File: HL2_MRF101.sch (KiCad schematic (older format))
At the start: 214 parts, among them J1 Antenna, J10 DB1, J2 HL2, J3 RF3, J4 RF1, J5 RCJ-041, J6 50VDC, J7 12V, J8 Fan, J9 HL2_12V, K1 EC2-3NU, K10 EC2-3NU, K11 EC2-3NU, K12 EC2-3NU, K13 EC2-3NU, K2 EC2-3NU, K3 EC2-3NU, K4 EC2-3NU, K5 EC2-3NU, K6 EC2-3NU, K7 EC2-3NU, K8 EC2-3NU, K9 EC2-3NU, Q1 MRF101AN, Q2 2N7002, Q3 IRLML6402, Q4 DTC144E, T1 Coupler, T2 Coupler, T3 744851330, U1 MCP6282E/MS, U2 MAX11645, U3 MCP23008, U4 ULN2003, U5 LM35-NEB, U6 MCP4561, U7 INA193

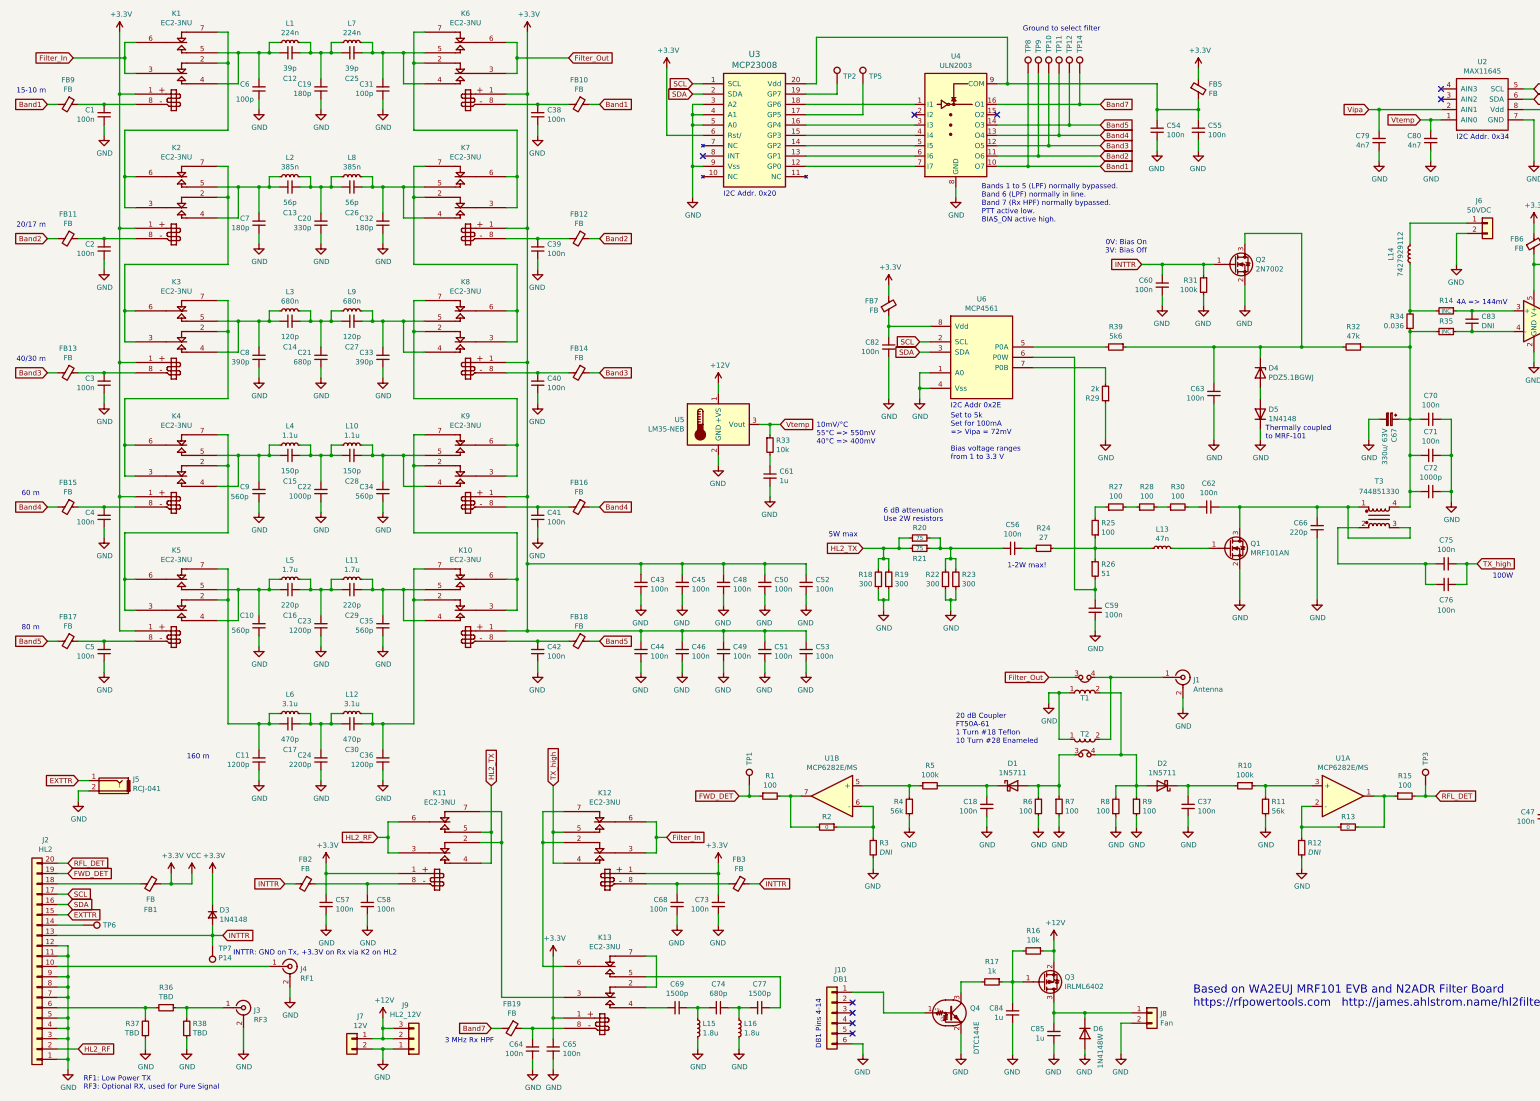
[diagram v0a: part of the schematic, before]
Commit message: Rx antenna change
RX antenna routed through HL2 rx antenna connection. High power tx tracks thickened to 2 mm and net list added for 50 ohm impedance top and bottom tracks for clearance.
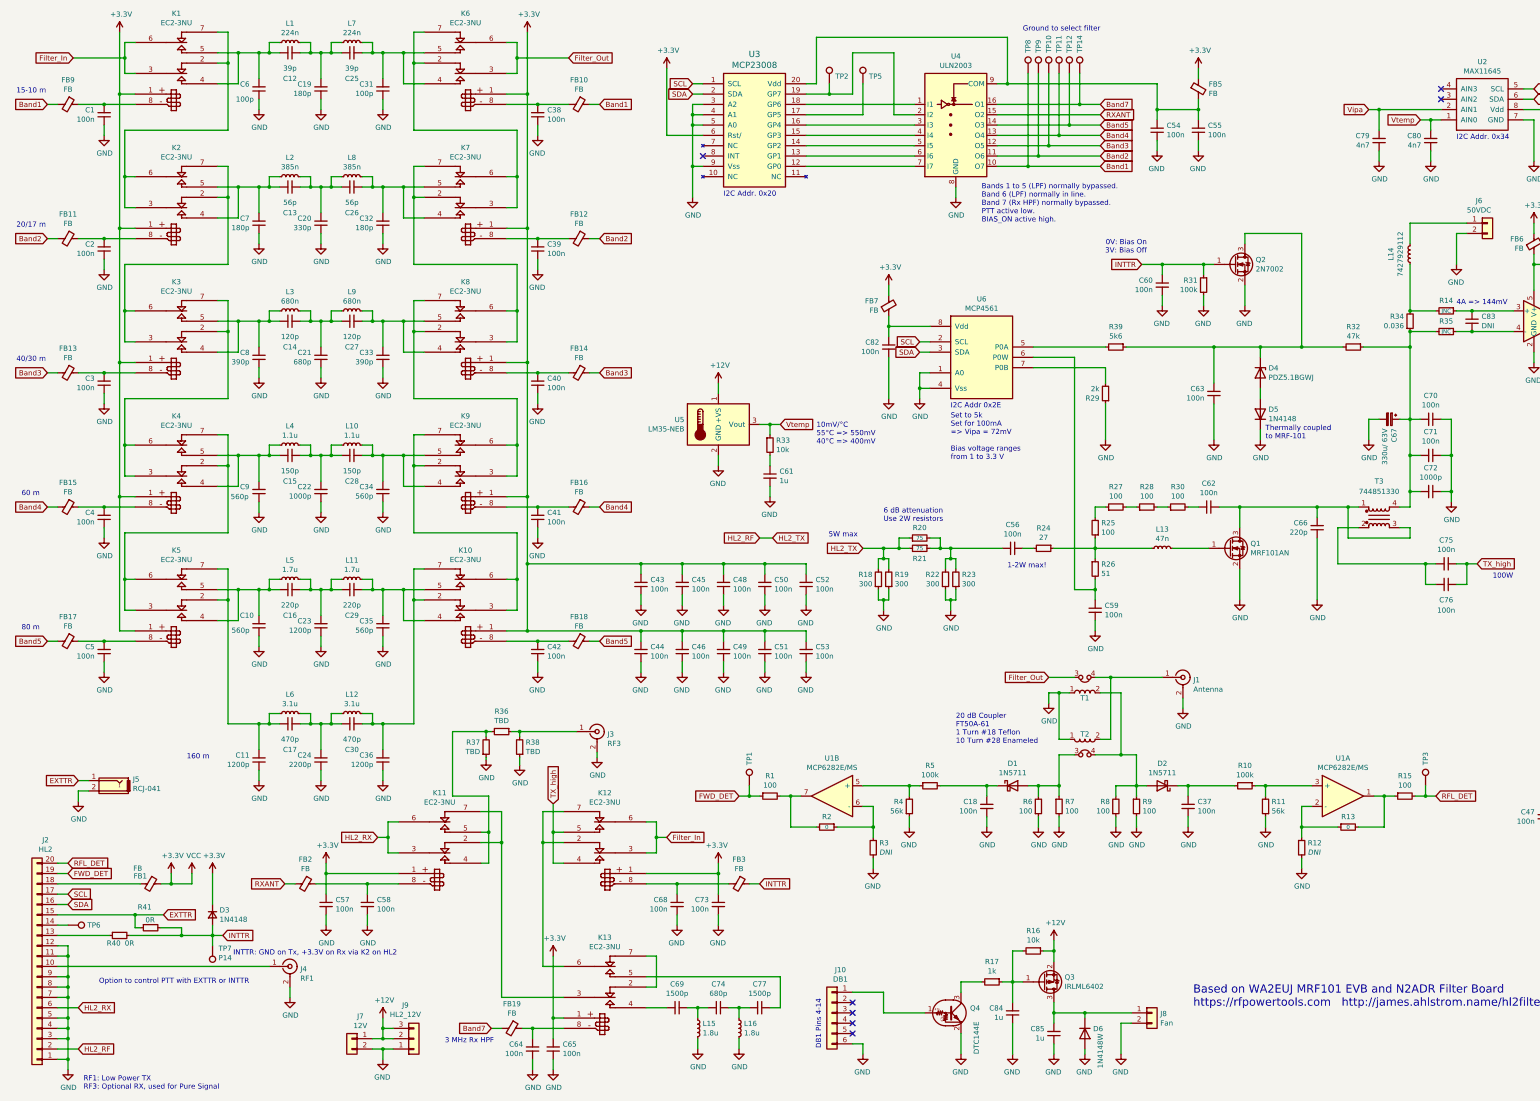
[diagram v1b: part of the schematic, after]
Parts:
- added R40, R41: 0R, Resistor_SMD:R_0603_1608Metric, symbol HL2_MRF101-rescue:R_Small-Device
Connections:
- net EXTTR: now also R41.1
- net HL2_RF: now also R18.2, R19.2, R20.1, R21.2; no longer K11.3, K11.6
- net INTTR: now also R40.2, R41.2; no longer FB2.2, J2.13 (Pin_13)
- net at R36.2, R37.2: now also K11.4, K11.5; no longer J2.6 (Pin_6)
- net at TP2.1, U3.19 (GP7): now also U4.2 (I2)
- net RXANT: now reaches U4.15 (O2)
- net RXANT: now also FB2.2
- removed net HL2_TX: K11.4, K11.5, R18.2, R19.2, R20.1, R21.2
- new net: J2.13 (Pin_13), R40.1
- new net HL2_RX: J2.6 (Pin_6), K11.3, K11.6
- no-connect marks 9 -> 7
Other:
- note added: "Option to control PTT with EXTTR or INTTR"
- moved on the sheet: J3, R36, R37, R38, TP2, TP6
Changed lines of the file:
@@
 Wire Wire Line
 	4100 8700 4100 8850
-Text GLabel 4000 8700 0    50   Input ~ 0
+Text GLabel 7700 5800 0    50   Input ~ 0
 HL2_RF
 Wire Wire Line
-	5000 8950 5100 8950
-Wire Wire Line
-	5100 8950 5100 8650
-Wire Wire Line
-	5100 8650 5000 8650
-Wire Wire Line
-	5100 8650 5100 8200
-Connection ~ 5100 8650
-Wire Wire Line
 	5800 8950 5700 8950
 Wire Wire Line
@@
 	5700 8650 5800 8650
 Wire Wire Line
-	5700 8650 5700 8200
+	5700 8650 5700 8375
 Connection ~ 5700 8650
 Wire Wire Line
@@
 Text GLabel 6800 8700 2    50   Input ~ 0
 Filter_In
-Text GLabel 5700 8200 1    50   Input ~ 0
+Text GLabel 5700 8375 1    50   Input ~ 0
 TX_high
-Text GLabel 5100 8200 1    50   Input ~ 0
+Text GLabel 7825 5800 2    50   Input ~ 0
 HL2_TX
 $Comp
@@
 $EndComp
 Text GLabel 3100 9150 0    50   Input ~ 0
-INTTR
+RXANT
 Wire Wire Line
 	3100 9150 3200 9150
@@
 SCL
 Wire Wire Line
-	900  9450 1000 9450
-Text GLabel 1000 9450 2    50   Input ~ 0
+	900  9450 1650 9450
+Text GLabel 1925 9450 2    50   Input ~ 0
 EXTTR
 $Comp
 L HL2_MRF101-rescue:TestPoint-Connector TP6
 U 1 1 60ED725B
-P 1150 9550
-F 0 "TP6" V 1150 9738 50  0000 L CNN
-F 1 "P8" V 1195 9738 50  0001 L CNN
-F 2 "TestPoint:TestPoint_Pad_D1.5mm" H 1350 9550 50  0001 C CNN
-F 3 "~" H 1350 9550 50  0001 C CNN
-	1    1150 9550
+P 1000 9550
+F 0 "TP6" V 1000 9738 50  0000 L CNN
+F 1 "P8" V 1045 9738 50  0001 L CNN
+F 2 "TestPoint:TestPoint_Pad_D1.5mm" H 1200 9550 50  0001 C CNN
+F 3 "~" H 1200 9550 50  0001 C CNN
+	1    1000 9550
 	0    1    1    0
 $EndComp
 Wire Wire Line
-	900  9550 1150 9550
+	900  9550 1000 9550
 $Comp
 L HL2_MRF101-rescue:TestPoint-Connector TP7
@@
 U 1 1 6126D5A4
 P 1800 9150
-F 0 "FB1" V 2050 9150 50  0000 C CNN
-F 1 "FB" V 1950 9150 50  0000 C CNN
+F 0 "FB1" V 1725 9050 50  0000 C CNN
+F 1 "FB" V 1650 9025 50  0000 C CNN
 F 2 "Inductor_SMD:L_0805_2012Metric" V 1730 9150 50  0001 C CNN
 F 3 "~" H 1800 9150 50  0001 C CNN
@@
 Wire Wire Line
 	900  9150 1700 9150
-Wire Wire Line
-	900  9650 2400 9650
 $Comp
 L HL2_MRF101-rescue:Conn_Coaxial-Connector J3
 U 1 1 5ECA38D8
-P 2700 10350
-F 0 "J3" H 2800 10325 50  0000 L CNN
-F 1 "RF3" H 2800 10234 50  0000 L CNN
-F 2 "n2adr:U.FL_Hirose_U.FL-R-SMT-1_Vertical" H 2700 10350 50  0001 C CNN
-F 3 " ~" H 2700 10350 50  0001 C CNN
-	1    2700 10350
+P 6125 7675
+F 0 "J3" H 6225 7650 50  0000 L CNN
+F 1 "RF3" H 6225 7559 50  0000 L CNN
+F 2 "n2adr:U.FL_Hirose_U.FL-R-SMT-1_Vertical" H 6125 7675 50  0001 C CNN
+F 3 " ~" H 6125 7675 50  0001 C CNN
+	1    6125 7675
 	1    0    0    -1
 $EndComp
@@
 Wire Wire Line
 	10800 1600 11000 1600
-NoConn ~ 10000 1700
-NoConn ~ 9200 1700
 Text Notes 8250 4900 0    50   ~ 0
 10mV/°C\n55°C => 550mV\n40°C => 400mV
@@
 L HL2_MRF101-rescue:R_Small-device R36
 U 1 1 5F471469
-P 1950 10350
-F 0 "R36" V 1754 10350 50  0000 C CNN
-F 1 "TBD" V 1845 10350 50  0000 C CNN
-F 2 "Resistor_SMD:R_0805_2012Metric" H 1950 10350 50  0001 C CNN
-F 3 "~" H 1950 10350 50  0001 C CNN
-	1    1950 10350
+P 5200 7675
+F 0 "R36" V 5004 7675 50  0000 C CNN
+F 1 "TBD" V 5095 7675 50  0000 C CNN
+F 2 "Resistor_SMD:R_0805_2012Metric" H 5200 7675 50  0001 C CNN
+F 3 "~" H 5200 7675 50  0001 C CNN
+	1    5200 7675
 	0    1    1    0
 $EndComp
@@
 L HL2_MRF101-rescue:R_Small-device R38
 U 1 1 5F4733D9
-P 2150 10550
-F 0 "R38" H 2091 10504 50  0000 R CNN
-F 1 "TBD" H 2091 10595 50  0000 R CNN
-F 2 "Resistor_SMD:R_0805_2012Metric" H 2150 10550 50  0001 C CNN
-F 3 "~" H 2150 10550 50  0001 C CNN
-	1    2150 10550
+P 5375 7825
+F 0 "R38" H 5316 7779 50  0000 R CNN
+F 1 "TBD" H 5316 7870 50  0000 R CNN
+F 2 "Resistor_SMD:R_0805_2012Metric" H 5375 7825 50  0001 C CNN
+F 3 "~" H 5375 7825 50  0001 C CNN
+	1    5375 7825
 	-1   0    0    1
 $EndComp
@@
 L HL2_MRF101-rescue:R_Small-device R37
 U 1 1 5F47390A
-P 1750 10550
-F 0 "R37" H 1692 10504 50  0000 R CNN
-F 1 "TBD" H 1692 10595 50  0000 R CNN
-F 2 "Resistor_SMD:R_0805_2012Metric" H 1750 10550 50  0001 C CNN
-F 3 "~" H 1750 10550 50  0001 C CNN
-	1    1750 10550
+P 5050 7825
+F 0 "R37" H 4992 7779 50  0000 R CNN
+F 1 "TBD" H 4992 7870 50  0000 R CNN
+F 2 "Resistor_SMD:R_0805_2012Metric" H 5050 7825 50  0001 C CNN
+F 3 "~" H 5050 7825 50  0001 C CNN
+	1    5050 7825
 	1    0    0    1
 $EndComp
@@
 L power:GND #PWR066
 U 1 1 5ECA38E2
-P 2700 10750
-F 0 "#PWR066" H 2700 10500 50  0001 C CNN
-F 1 "GND" H 2705 10577 50  0000 C CNN
-F 2 "" H 2700 10750 50  0001 C CNN
-F 3 "" H 2700 10750 50  0001 C CNN
-	1    2700 10750
+P 6125 7925
+F 0 "#PWR066" H 6125 7675 50  0001 C CNN
+F 1 "GND" H 6130 7752 50  0000 C CNN
+F 2 "" H 6125 7925 50  0001 C CNN
+F 3 "" H 6125 7925 50  0001 C CNN
+	1    6125 7925
 	1    0    0    -1
 $EndComp
@@
 L power:GND #PWR0107
 U 1 1 5F52250E
-P 2150 10750
-F 0 "#PWR0107" H 2150 10500 50  0001 C CNN
-F 1 "GND" H 2155 10577 50  0000 C CNN
-F 2 "" H 2150 10750 50  0001 C CNN
-F 3 "" H 2150 10750 50  0001 C CNN
-	1    2150 10750
+P 5375 8000
+F 0 "#PWR0107" H 5375 7750 50  0001 C CNN
+F 1 "GND" H 5380 7827 50  0000 C CNN
+F 2 "" H 5375 8000 50  0001 C CNN
+F 3 "" H 5375 8000 50  0001 C CNN
+	1    5375 8000
 	1    0    0    -1
 $EndComp
 Wire Wire Line
-	2150 10650 2150 10750
+	5375 7925 5375 8000
 $Comp
 L power:GND #PWR0109
 U 1 1 5F5D17C4
-P 1750 10750
-F 0 "#PWR0109" H 1750 10500 50  0001 C CNN
-F 1 "GND" H 1755 10577 50  0000 C CNN
-F 2 "" H 1750 10750 50  0001 C CNN
-F 3 "" H 1750 10750 50  0001 C CNN
-	1    1750 10750
+P 5050 7950
+F 0 "#PWR0109" H 5050 7700 50  0001 C CNN
+F 1 "GND" H 5055 7777 50  0000 C CNN
+F 2 "" H 5050 7950 50  0001 C CNN
+F 3 "" H 5050 7950 50  0001 C CNN
+	1    5050 7950
 	1    0    0    -1
 $EndComp
 Wire Wire Line
-	1750 10650 1750 10750
-Wire Wire Line
-	2050 10350 2150 10350
+	5050 7925 5050 7950
 Wire Wire Line
-	2150 10350 2150 10450
-Wire Wire Line
-	2150 10350 2500 10350
-Connection ~ 2150 10350
-Wire Wire Line
-	2700 10550 2700 10750
+	6125 7875 6125 7925
 $Comp
 L HL2_MRF101-rescue:Ferrite_Bead_Small-Device FB19
@@
 	1    0    0    1
 $EndComp
-$Comp
-L HL2_MRF101-rescue:TestPoint-Connector TP2
-U 1 1 603E8483
-P 8450 1400
-F 0 "TP2" H 8508 1472 50  0000 L CNN
-F 1 "P8" V 8495 1588 50  0001 L CNN
-F 2 "TestPoint:TestPoint_Pad_D1.5mm" H 8650 1400 50  0001 C CNN
-F 3 "~" H 8650 1400 50  0001 C CNN
-	1    8450 1400
-	1    0    0    -1
-$EndComp
 Wire Wire Line
-	8150 1500 8450 1500
-Wire Wire Line
-	8450 1500 8450 1400
+	8375 1500 8375 1400
 $Comp
 L HL2_MRF101-rescue:C_Small-device C85
@@
 Wire Wire Line
 	10550 10400 10850 10400
-Wire Wire Line
-	900  10350 1750 10350
-Wire Wire Line
-	1750 10450 1750 10350
-Connection ~ 1750 10350
-Wire Wire Line
-	1750 10350 1850 10350
 $Comp
 L power:GND #PWR061
@@
 	14000 3150 14000 3600
 Connection ~ 14000 3600
+$Comp
+L HL2_MRF101-rescue:TestPoint-Connector TP2
+U 1 1 603E8483
+P 8375 1400
+F 0 "TP2" H 8433 1472 50  0000 L CNN
+F 1 "P8" V 8420 1588 50  0001 L CNN
+F 2 "TestPoint:TestPoint_Pad_D1.5mm" H 8575 1400 50  0001 C CNN
+F 3 "~" H 8575 1400 50  0001 C CNN
+	1    8375 1400
+	1    0    0    -1
+$EndComp
+Wire Wire Line
+	9200 1700 9000 1700
+Wire Wire Line
+	9000 1700 9000 1100
+Wire Wire Line
+	9000 1100 8600 1100
+Wire Wire Line
+	8600 1100 8600 1500
+Wire Wire Line
+	8150 1500 8375 1500
+Connection ~ 8375 1500
+Wire Wire Line
+	8375 1500 8600 1500
+Wire Wire Line
+	10000 1700 11000 1700
+Text GLabel 11000 1700 2    50   Input ~ 0
+RXANT
+Wire Wire Line
+	7700 5800 7825 5800
+Wire Wire Line
+	5000 8650 5075 8650
+Wire Wire Line
+	5075 8650 5075 8950
+Wire Wire Line
+	5075 8950 5000 8950
+Wire Wire Line
+	5075 8650 5075 8300
+Wire Wire Line
+	5075 8300 4725 8300
+Wire Wire Line
+	4725 8300 4725 7675
+Connection ~ 5075 8650
+Text GLabel 1100 10350 2    50   Input ~ 0
+HL2_RX
+Text GLabel 4000 8700 0    50   Input ~ 0
+HL2_RX
+Wire Wire Line
+	900  10350 1100 10350
+Wire Wire Line
+	5300 7675 5375 7675
+Wire Wire Line
+	5375 7725 5375 7675
+Connection ~ 5375 7675
+Wire Wire Line
+	5375 7675 5925 7675
+Wire Wire Line
+	5050 7725 5050 7675
+Connection ~ 5050 7675
+Wire Wire Line
+	5050 7675 5100 7675
+Wire Wire Line
+	4725 7675 5050 7675
+$Comp
+L HL2_MRF101-rescue:R_Small-Device R40
+U 1 1 5F0CA10F
+P 1500 9650
+F 0 "R40" V 1575 9775 50  0000 R CNN
+F 1 "0R" V 1575 9600 50  0000 R CNN
+F 2 "Resistor_SMD:R_0603_1608Metric" H 1500 9650 50  0001 C CNN
+F 3 "~" H 1500 9650 50  0001 C CNN
+	1    1500 9650
+	0    -1   1    0
+$EndComp
+Wire Wire Line
+	900  9650 1400 9650
+Wire Wire Line
+	1600 9650 2100 9650
+$Comp
+L HL2_MRF101-rescue:R_Small-Device R41
+U 1 1 5F319C99
+P 1800 9575
+F 0 "R41" V 1600 9700 50  0000 R CNN
+F 1 "0R" V 1725 9625 50  0000 R CNN
+F 2 "Resistor_SMD:R_0603_1608Metric" H 1800 9575 50  0001 C CNN
+F 3 "~" H 1800 9575 50  0001 C CNN
+	1    1800 9575
+	0    -1   1    0
+$EndComp
+Wire Wire Line
+	1900 9575 2100 9575
+Wire Wire Line
+	2100 9575 2100 9650
+Connection ~ 2100 9650
+Wire Wire Line
+	2100 9650 2400 9650
+Wire Wire Line
+	1700 9575 1650 9575
+Wire Wire Line
+	1650 9575 1650 9450
+Connection ~ 1650 9450
+Wire Wire Line
+	1650 9450 1925 9450
+Text Notes 1300 10125 0    50   ~ 0
+Option to control PTT with EXTTR or INTTR
 Wire Wire Line
-	14000 2750 14550 2750
+	14550 2750 14000 2750
 $EndSCHEMATC

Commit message: Update relays
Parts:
- removed TP10, TP11, TP12, TP14, TP2, TP8, TP9: P8, TestPoint:TestPoint_Pad_D1.5mm, symbol HL2_MRF101-rescue:TestPoint-Connector
- C14, C27: value 120p -> 100p
- C21: value 680p -> 470p
- C33, C8: value 390p -> 270p
- D5: footprint Diode_THT:D_DO-35_SOD27_P7.62mm_Horizontal -> Diode_THT:D_DO-35_SOD27_P2.54mm_Vertical_KathodeUp
- J10: footprint Pin_Headers:Pin_Header_Straight_1x06_Pitch2.54mm -> Connector_PinHeader_2.54mm:PinHeader_1x06_P2.54mm_Vertical
- K1, K10, K12, K2, K3, K4, K5, K6, K7, K8, K9: value EC2-3NU -> AXICOM D2N; footprint n2adr:RelayDPDT01 -> n2adr:RelayDPDT02
- K11, K13: value EC2-3NU -> EC2-12NU
- L3, L9: value 680n -> 710n
- Q3, Q4: footprint TO_SOT_Packages_SMD:SOT-23 -> Package_TO_SOT_SMD:SOT-23
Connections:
- net +12V: now also C43.2, C44.2, C45.2, C46.2, C48.2, C49.2, C50.2, C51.2, C52.2, C53.2, C57.1, C65.2, C73.1, FB5.1, K1.1, K10.1, K11.1, K12.1, K13.1, K2.1, K3.1, K4.1, K5.1, K6.1, K7.1, K8.1, K9.1
- net +3V3: now also C54.2, U3.20 (Vdd); no longer C43.2, C44.2, C45.2, C46.2, C48.2, C49.2, C50.2, C51.2, C52.2, C53.2, C57.1, C65.2, C73.1, FB5.1, K1.1, K10.1, K11.1, K12.1, K13.1, K2.1, K3.1, K4.1, K5.1, K6.1, K7.1, K8.1, K9.1
- net at C55.2, FB5.2, U4.9 (COM): no longer C54.2, U3.20 (Vdd)
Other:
- note added: "Bands 1 to 5 (LPF) normally bypassed.\nBand 7 (Rx HPF) normally bypassed.\nRXANT, normall off"
- note added: "DO NOT SUBSTITUTE"
- note added: "RF1: Low Power TX\n"
- note added: "RF3: RX antenna, (or for Pure Signal)"
- note removed: "Bands 1 to 5 (LPF) normally bypassed.\nBand 6 (LPF) normally in line.\nBand 7 (Rx HPF) normally bypassed.\nPTT active low.\nBIAS_ON active high."
- note removed: "RF1: Low Power TX\nRF3: Optional RX, used for Pure Signal"
- moved on the sheet: C54
